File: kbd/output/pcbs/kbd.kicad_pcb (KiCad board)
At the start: 2 copper layers, 168.7 x 132.5 mm, 29 parts

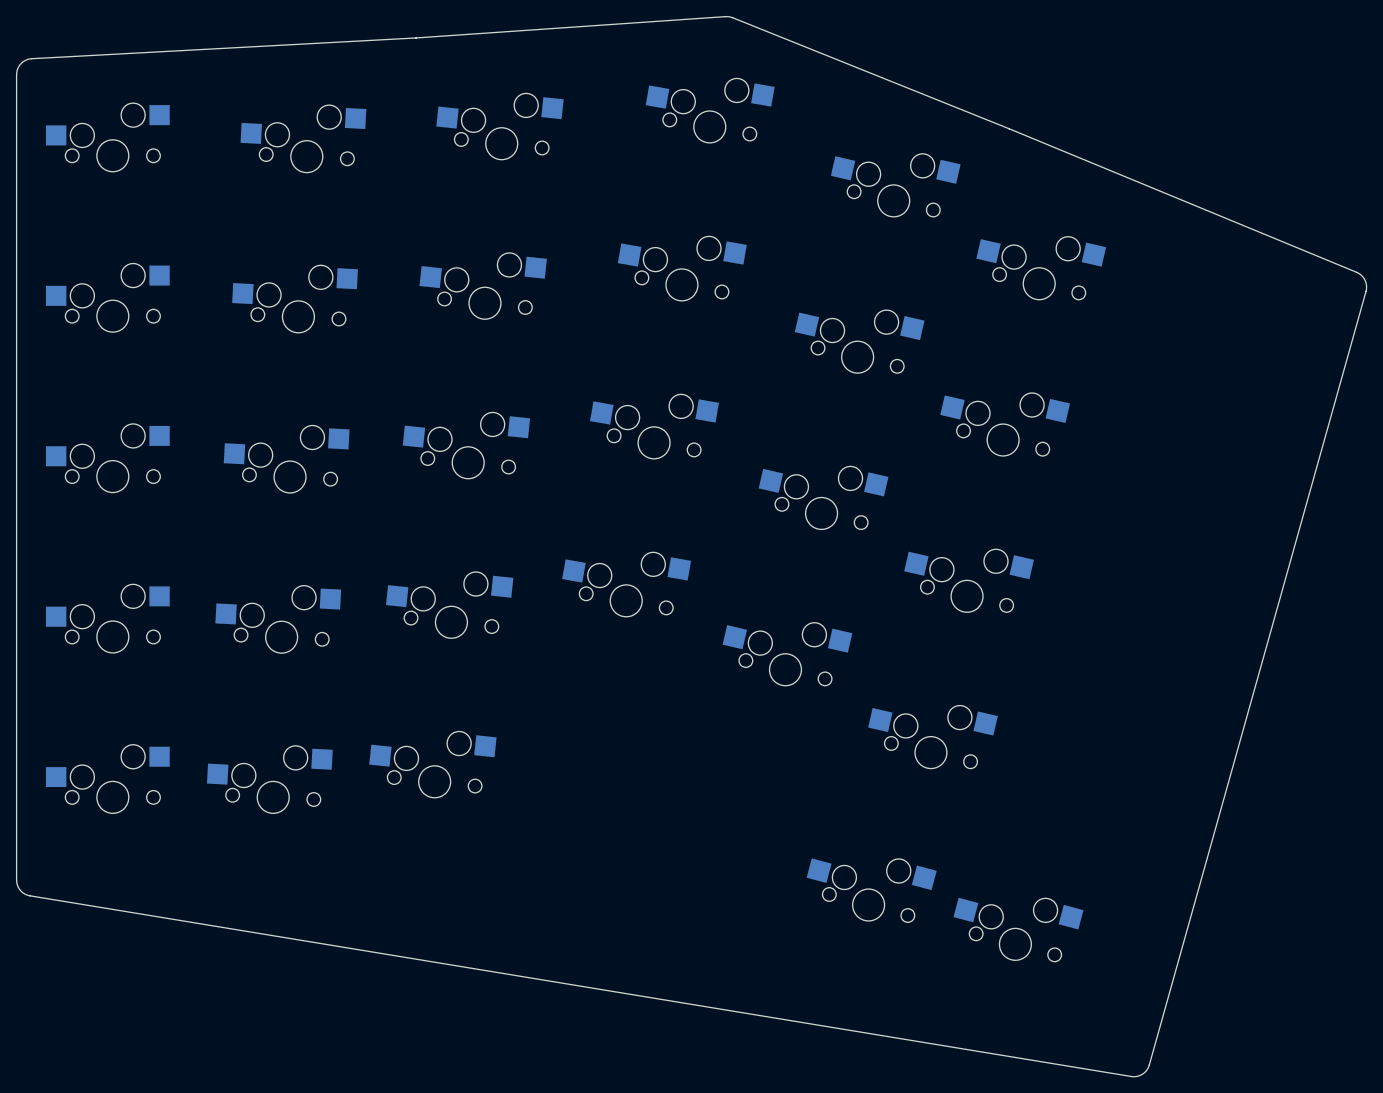
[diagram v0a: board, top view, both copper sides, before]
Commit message: added mcu jack and reset
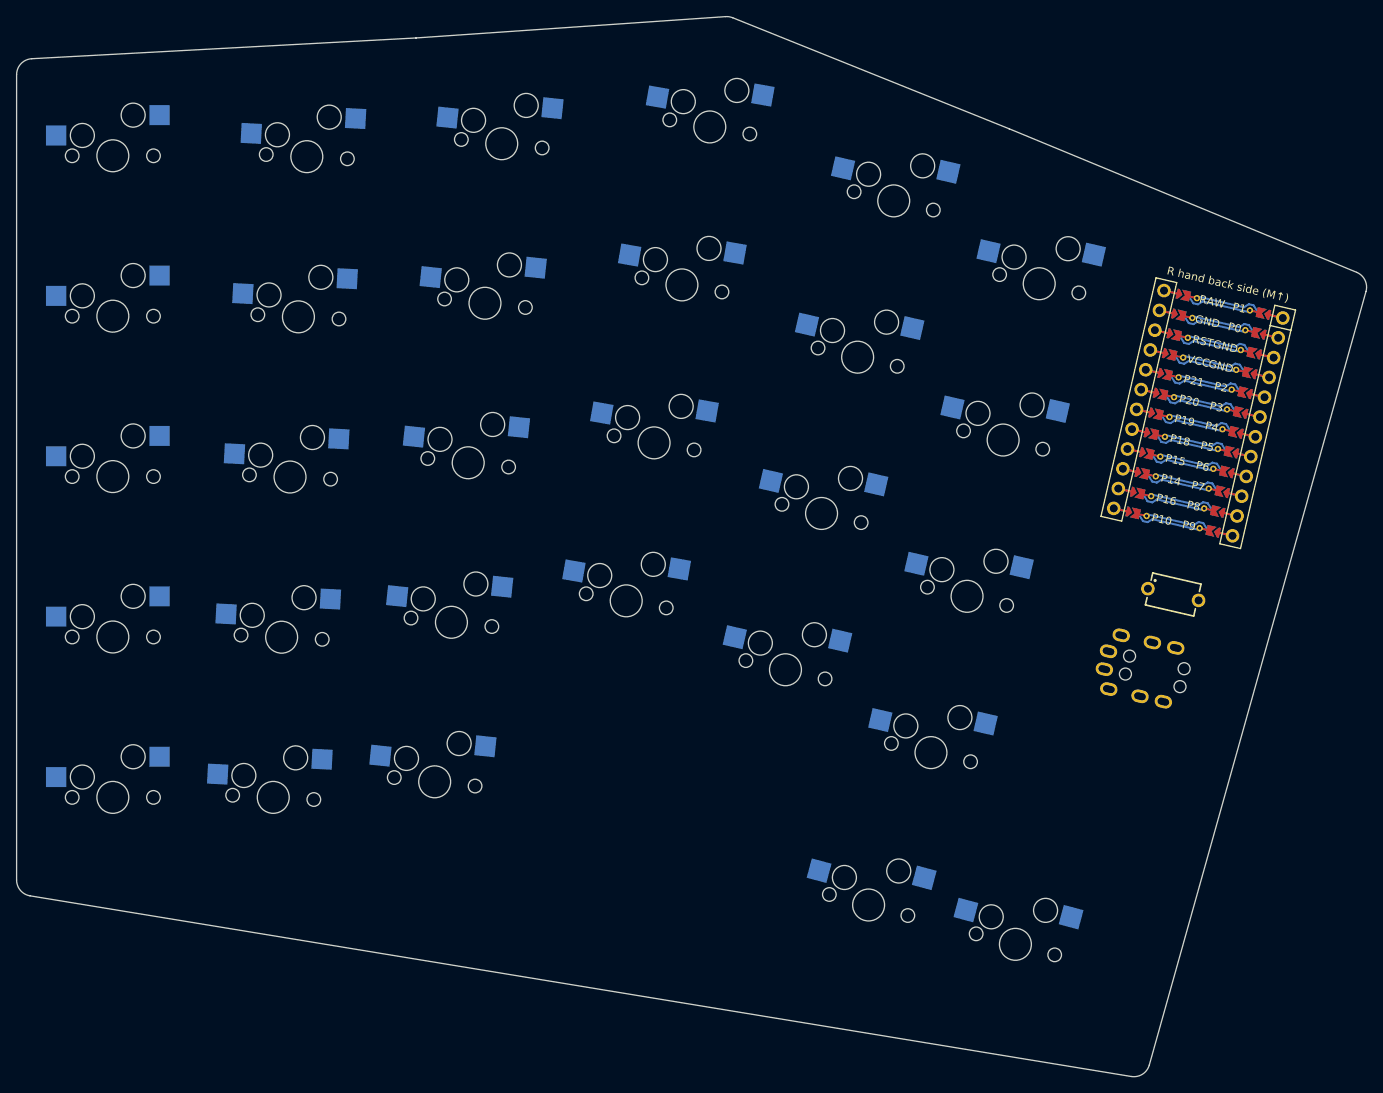
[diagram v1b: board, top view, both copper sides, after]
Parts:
- added MCU1: , ceoloide:mcu_supermini_nrf52840, F.Cu at (286.0, 100.7)
- added S30: , 434121025816, F.Cu at (282.5, 124.6)
- added TRRS1: TRRS-PJ-320A-dual, TRRS-PJ-320A-dual, F.Cu at (285.0, 136.5)
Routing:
- net (no net): track 0.00 -> 337.7 mm
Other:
- net class Default added: clearance 0.2, trace_width 0.25, via_dia 0.8, via_drill 0.4

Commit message: configured jack better
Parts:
- TRRS1: value TRRS-PJ-320A-dual -> (none); footprint TRRS-PJ-320A-dual -> ceoloide:trrs_pj320a (reversible, symmetric)
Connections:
- TRRS1 pad 2: (no net) -> GND
- TRRS1 pad 3: (no net) -> P0
- TRRS1 pad 4: (no net) -> VCC
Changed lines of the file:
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@@
             (pad 2 thru_hole oval (at 3.25 0.0 -13) (size 1.7 1.7) (drill 1) (layers *.Cu *.Mask) (net 31 "GND"))
         )
-      (module TRRS-PJ-320A-dual (layer F.Cu)
-      (at 284.953054 136.51600059999998 -103)
-      (fp_text reference "TRRS1" (at 0 14.2) (layer Dwgs.User) (effects (font (size 1 1) (thickness 0.15))))
-      (fp_text value TRRS-PJ-320A-dual (at 0 -5.6) (layer F.Fab) (effects (font (size 1 1) (thickness 0.15))))
-      (fp_line (start 0.5 -2) (end -5.1 -2) (layer Dwgs.User) (width 0.15))
-      (fp_line (start -5.1 0) (end -5.1 -2) (layer Dwgs.User) (width 0.15))
-      (fp_line (start 0.5 0) (end 0.5 -2) (layer Dwgs.User) (width 0.15))
-      (fp_line (start -5.35 0) (end -5.35 12.1) (layer Dwgs.User) (width 0.15))
-      (fp_line (start 0.75 0) (end 0.75 12.1) (layer Dwgs.User) (width 0.15))
-      (fp_line (start 0.75 12.1) (end -5.35 12.1) (layer Dwgs.User) (width 0.15))
-      (fp_line (start 0.75 0) (end -5.35 0) (layer Dwgs.User) (width 0.15))
-        (pad "" np_thru_hole circle (at -2.3 8.6) (size 1.5 1.5) (drill 1.5) (layers *.Cu *.Mask))
-        (pad "" np_thru_hole circle (at -2.3 1.6) (size 1.5 1.5) (drill 1.5) (layers *.Cu *.Mask))
-        (pad "" np_thru_hole circle (at 0 8.6) (size 1.5 1.5) (drill 1.5) (layers *.Cu *.Mask))
-        (pad "" np_thru_hole circle (at 0 1.6) (size 1.5 1.5) (drill 1.5) (layers *.Cu *.Mask))
-        (pad 1 thru_hole oval (at -2.3 11.3 -103) (size 1.6 2.2) (drill oval 0.9 1.5) (layers *.Cu *.Mask) (net 0 ""))
-        (pad 2 thru_hole oval (at 2.3 10.2 -103) (size 1.6 2.2) (drill oval 0.9 1.5) (layers *.Cu *.Mask) (net 0 ""))
-        (pad 3 thru_hole oval (at 2.3 6.2 -103) (size 1.6 2.2) (drill oval 0.9 1.5) (layers *.Cu *.Mask) (net 0 ""))
-        (pad 4 thru_hole oval (at 2.3 3.2 -103) (size 1.6 2.2) (drill oval 0.9 1.5) (layers *.Cu *.Mask) (net 0 ""))
-        (pad 1 thru_hole oval (at 0 11.3 -103) (size 1.6 2.2) (drill oval 0.9 1.5) (layers *.Cu *.Mask) (net 0 ""))
-        (pad 2 thru_hole oval (at -4.6 10.2 -103) (size 1.6 2.2) (drill oval 0.9 1.5) (layers *.Cu *.Mask) (net 0 ""))
-        (pad 3 thru_hole oval (at -4.6 6.2 -103) (size 1.6 2.2) (drill oval 0.9 1.5) (layers *.Cu *.Mask) (net 0 ""))
-        (pad 4 thru_hole oval (at -4.6 3.2 -103) (size 1.6 2.2) (drill oval 0.9 1.5) (layers *.Cu *.Mask) (net 0 ""))
-      )
+  (footprint "ceoloide:trrs_pj320a (reversible, symmetric)"
+    (layer "F.Cu")
+    (at 284.953054 136.51600059999998 -103)
+    (property "Reference" "TRRS1"
+      (at 0 14.2 -103)
+      (layer "F.SilkS")
+      hide
+      (effects (font (size 1 1) (thickness 0.15)))
+    )
+    (fp_line (start 2.8 -2) (end -2.8 -2) (layer "Dwgs.User") (stroke (width 0.15) (type solid)))
+    (fp_line (start -2.8 0) (end -2.8 -2) (layer "Dwgs.User") (stroke (width 0.15) (type solid)))
+    (fp_line (start 2.8 0) (end 2.8 -2) (layer "Dwgs.User") (stroke (width 0.15) (type solid)))
+    (fp_line (start -3.05 0) (end -3.05 12.1) (layer "Dwgs.User") (stroke (width 0.15) (type solid)))
+    (fp_line (start 3.05 0) (end 3.05 12.1) (layer "Dwgs.User") (stroke (width 0.15) (type solid)))
+    (fp_line (start 3.05 12.1) (end -3.05 12.1) (layer "Dwgs.User") (stroke (width 0.15) (type solid)))
+    (fp_line (start 3.05 0) (end -3.05 0) (layer "Dwgs.User") (stroke (width 0.15) (type solid)))
+    (pad "" np_thru_hole circle (at 0 8.6 -103) (size 1.5 1.5) (drill 1.5) (layers "*.Cu" "*.Mask"))
+    (pad "" np_thru_hole circle (at 0 1.6 -103) (size 1.5 1.5) (drill 1.5) (layers "*.Cu" "*.Mask"))
+    (pad 2 thru_hole oval (at -2.3 3.2 -103) (size 1.6 2.2) (drill oval 0.9 1.5) (layers "*.Cu" "*.Mask") (net 31 "GND"))
+    (pad 3 thru_hole oval (at -2.3 6.2 -103) (size 1.6 2.2) (drill oval 0.9 1.5) (layers "*.Cu" "*.Mask") (net 43 "P0"))
+    (pad 4 thru_hole oval (at -2.3 10.75 -103) (size 1.6 3.3) (drill oval 0.9 2.6) (layers "*.Cu" "*.Mask") (net 33 "VCC"))
+    (pad 2 thru_hole oval (at 2.3 3.2 -103) (size 1.6 2.2) (drill oval 0.9 1.5) (layers "*.Cu" "*.Mask") (net 31 "GND"))
+    (pad 3 thru_hole oval (at 2.3 6.2 -103) (size 1.6 2.2) (drill oval 0.9 1.5) (layers "*.Cu" "*.Mask") (net 43 "P0"))
+    (pad 4 thru_hole oval (at 2.3 10.75 -103) (size 1.6 3.3) (drill oval 0.9 2.6) (layers "*.Cu" "*.Mask") (net 33 "VCC"))
+  )
   (gr_line (start 137.97 160.33137438513705) (end 137.97 59.66482912375419) (angle 90) (layer Edge.Cuts) (width 0.15))
 (gr_line (start 139.86206800538875 57.66774362346295) (end 187.89129481507507 55.07201519961849) (angle 90) (layer Edge.Cuts) (width 0.15))

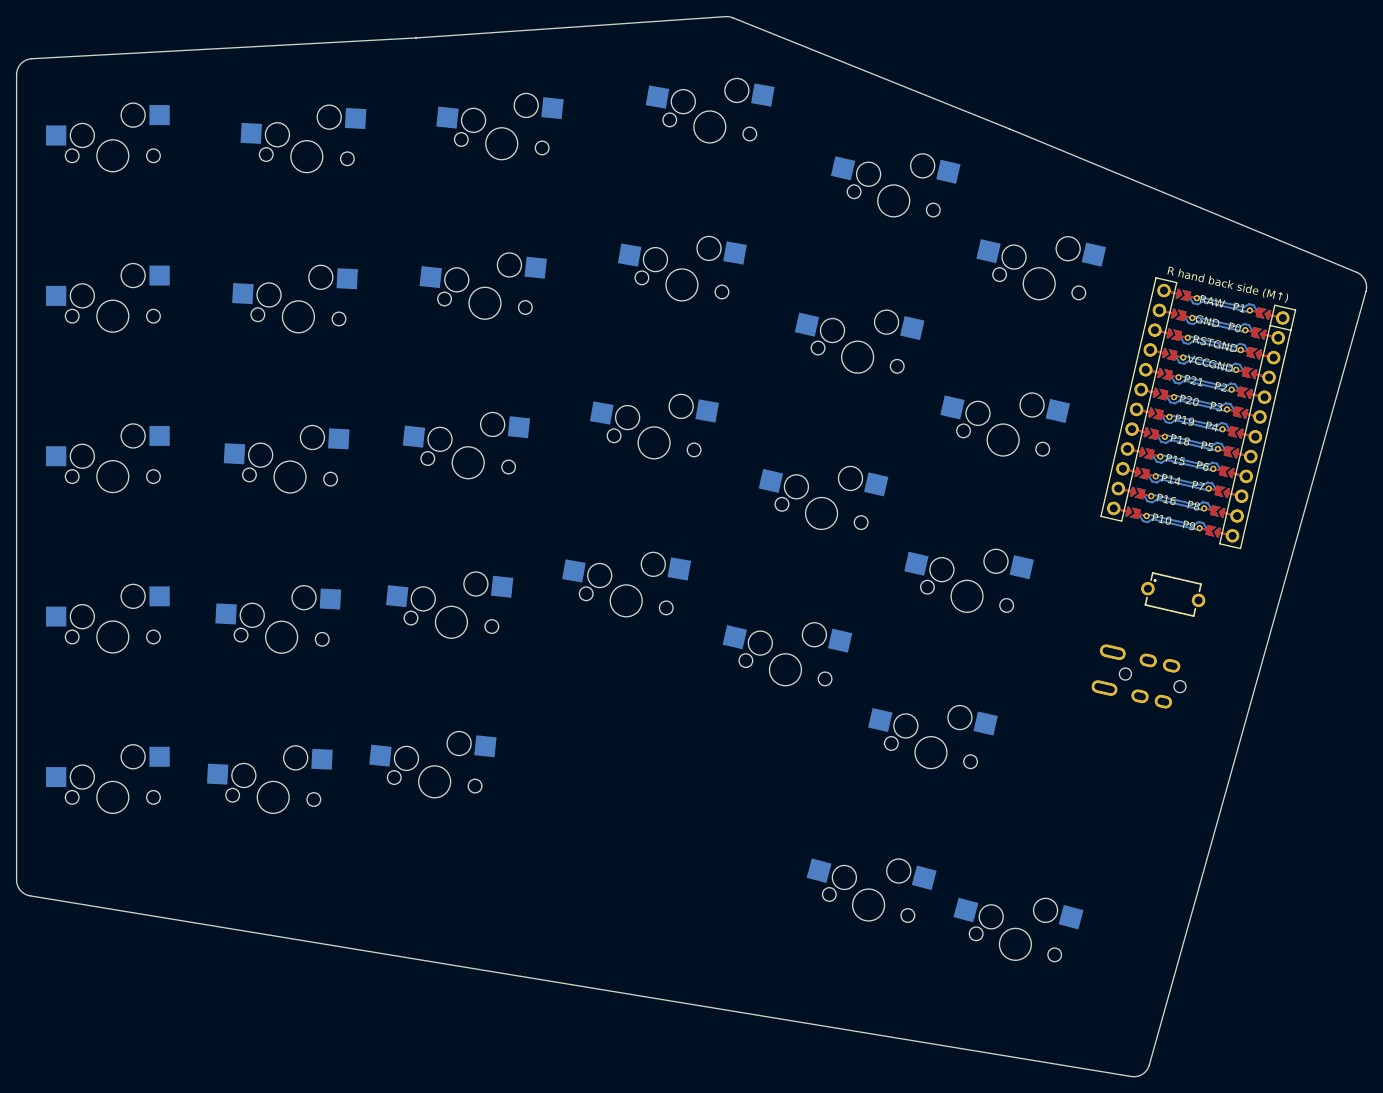
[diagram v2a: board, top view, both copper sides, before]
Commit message: added key net/matrix
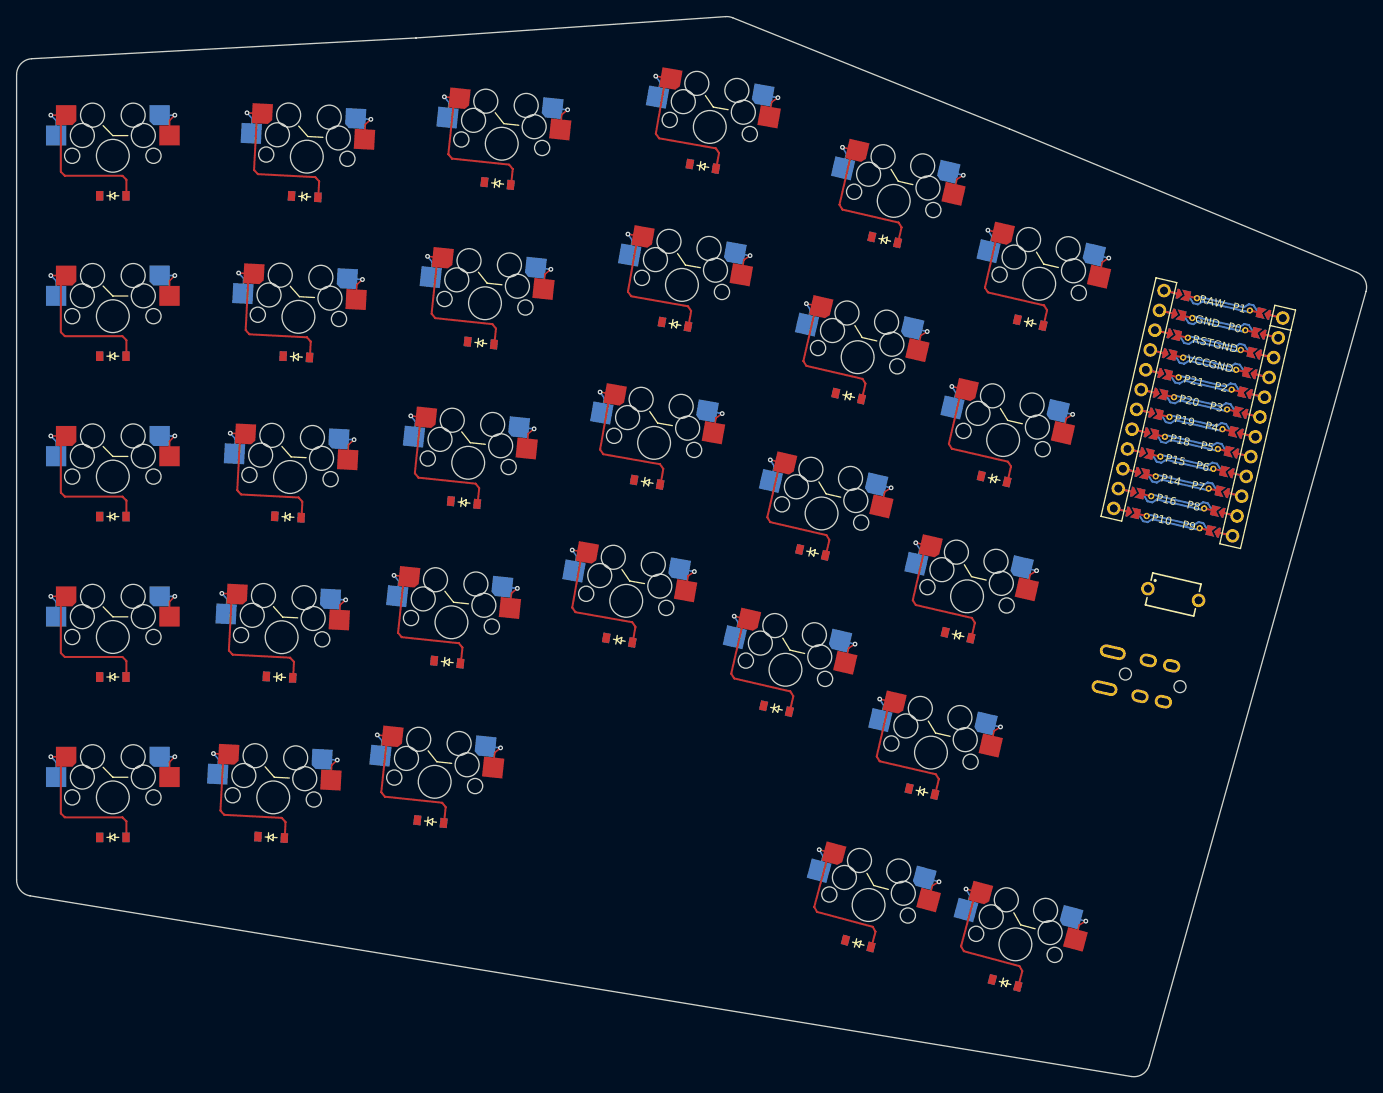
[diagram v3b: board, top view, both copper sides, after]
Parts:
- added D1: , ceoloide:diode_tht_sod123, F.Cu at (150.0, 155.0)
- added D10: , ceoloide:diode_tht_sod123, F.Cu at (174.0, 74.9)
- added D11: , ceoloide:diode_tht_sod123, F.Cu at (189.7, 153.0)
- added D12: , ceoloide:diode_tht_sod123, F.Cu at (191.8, 133.1)
- added D13: , ceoloide:diode_tht_sod123, F.Cu at (193.9, 113.1)
- added D14: , ceoloide:diode_tht_sod123, F.Cu at (196.0, 93.2)
- added D15: , ceoloide:diode_tht_sod123, F.Cu at (198.1, 73.3)
- added D16: , ceoloide:diode_tht_sod123, F.Cu at (213.3, 130.4)
- added D17: , ceoloide:diode_tht_sod123, F.Cu at (216.8, 110.6)
- added D18: , ceoloide:diode_tht_sod123, F.Cu at (220.3, 90.9)
- added D19: , ceoloide:diode_tht_sod123, F.Cu at (223.8, 71.1)
- added D2: , ceoloide:diode_tht_sod123, F.Cu at (150.0, 134.9)
- added D20: , ceoloide:diode_tht_sod123, F.Cu at (233.0, 138.9)
- added D21: , ceoloide:diode_tht_sod123, F.Cu at (237.5, 119.4)
- added D22: , ceoloide:diode_tht_sod123, F.Cu at (242.0, 99.8)
- added D23: , ceoloide:diode_tht_sod123, F.Cu at (246.5, 80.3)
- added D24: , ceoloide:diode_tht_sod123, F.Cu at (251.1, 149.3)
- added D25: , ceoloide:diode_tht_sod123, F.Cu at (255.7, 129.7)
- added D26: , ceoloide:diode_tht_sod123, F.Cu at (260.2, 110.2)
- added D27: , ceoloide:diode_tht_sod123, F.Cu at (264.7, 90.7)
- added D28: , ceoloide:diode_tht_sod123, F.Cu at (243.2, 168.3)
- added D29: , ceoloide:diode_tht_sod123, F.Cu at (261.5, 173.2)
- added D3: , ceoloide:diode_tht_sod123, F.Cu at (150.0, 114.9)
- added D4: , ceoloide:diode_tht_sod123, F.Cu at (150.0, 94.8)
- added D5: , ceoloide:diode_tht_sod123, F.Cu at (150.0, 74.8)
- added D6: , ceoloide:diode_tht_sod123, F.Cu at (169.8, 155.0)
- added D7: , ceoloide:diode_tht_sod123, F.Cu at (170.8, 135.0)
- added D8: , ceoloide:diode_tht_sod123, F.Cu at (171.9, 114.9)
- added D9: , ceoloide:diode_tht_sod123, F.Cu at (172.9, 94.9)
- S1, S10, S11, S12, S13, S14, S15, S16, S17, S18, S19, S2, S20, S21, S22, S23, S24, S25, S26, S27, S28, S29, S3, S4, S5, S6, S7, S8, S9: footprint MX -> ceoloide:switch_mx; moved to B.Cu
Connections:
- S1 pad 1: (no net) -> outer_mod
- S1 pad 2: outer_mod -> P4
- S10 pad 1: (no net) -> pinky_num
- S10 pad 2: pinky_num -> P5
- S11 pad 1: (no net) -> ring_mod
- S11 pad 2: ring_mod -> P6
- S12 pad 1: (no net) -> ring_bottom
- S12 pad 2: ring_bottom -> P6
- S13 pad 1: (no net) -> ring_home
- S13 pad 2: ring_home -> P6
- S14 pad 1: (no net) -> ring_top
- S14 pad 2: ring_top -> P6
- S15 pad 1: (no net) -> ring_num
- S15 pad 2: ring_num -> P6
- S16 pad 1: (no net) -> middle_bottom
- S16 pad 2: middle_bottom -> P7
- S17 pad 1: (no net) -> middle_home
- S17 pad 2: middle_home -> P7
- S18 pad 1: (no net) -> middle_top
- S18 pad 2: middle_top -> P7
- S19 pad 1: (no net) -> middle_num
- S19 pad 2: middle_num -> P7
- S2 pad 1: (no net) -> outer_bottom
- S2 pad 2: outer_bottom -> P4
- S20 pad 1: (no net) -> index_bottom
- S20 pad 2: index_bottom -> P8
- S21 pad 1: (no net) -> index_home
- S21 pad 2: index_home -> P8
- S22 pad 1: (no net) -> index_top
- S22 pad 2: index_top -> P8
- S23 pad 1: (no net) -> index_num
- S23 pad 2: index_num -> P8
- S24 pad 1: (no net) -> inner_bottom
- S24 pad 2: inner_bottom -> P9
- S25 pad 1: (no net) -> inner_home
- S25 pad 2: inner_home -> P9
- S26 pad 1: (no net) -> inner_top
- S26 pad 2: inner_top -> P9
- S27 pad 1: (no net) -> inner_num
- S27 pad 2: inner_num -> P9
- S28 pad 1: (no net) -> layer_cluster
- S28 pad 2: layer_cluster -> P8
- S29 pad 1: (no net) -> space_cluster
- S29 pad 2: space_cluster -> P9
- S3 pad 1: (no net) -> outer_home
- S3 pad 2: outer_home -> P4
- S4 pad 1: (no net) -> outer_top
- S4 pad 2: outer_top -> P4
- S5 pad 1: (no net) -> outer_num
- S5 pad 2: outer_num -> P4
- S6 pad 1: (no net) -> pinky_mod
- S6 pad 2: pinky_mod -> P5
- S7 pad 1: (no net) -> pinky_bottom
- S7 pad 2: pinky_bottom -> P5
- S8 pad 1: (no net) -> pinky_home
- S8 pad 2: pinky_home -> P5
- S9 pad 1: (no net) -> pinky_top
- S9 pad 2: pinky_top -> P5
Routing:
- net (no net): track 337.7 -> 856.2 mm
- net P8: track 0.00 -> 23.6 mm, vias 0 -> 5
- net P9: track 0.00 -> 23.6 mm, vias 0 -> 5
- net P5: track 0.00 -> 23.6 mm, vias 0 -> 5
- net P4: track 0.00 -> 23.6 mm, vias 0 -> 5
- net P6: track 0.00 -> 23.6 mm, vias 0 -> 5
- net P7: track 0.00 -> 18.9 mm, vias 0 -> 4
- net space_cluster: track 0.00 -> 4.72 mm, vias 0 -> 1
- net layer_cluster: track 0.00 -> 4.72 mm, vias 0 -> 1
- net outer_mod: track 0.00 -> 4.72 mm, vias 0 -> 1
- net outer_top: track 0.00 -> 4.72 mm, vias 0 -> 1
- net outer_num: track 0.00 -> 4.72 mm, vias 0 -> 1
- net outer_home: track 0.00 -> 4.72 mm, vias 0 -> 1
- net outer_bottom: track 0.00 -> 4.72 mm, vias 0 -> 1
- net middle_top: track 0.00 -> 4.72 mm, vias 0 -> 1
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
